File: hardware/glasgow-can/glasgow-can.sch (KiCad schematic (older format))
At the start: 19 parts, among them J1 2834077-2, J10 pkl_jumper_nc, J11 pkl_jumper_nc, J12 pkl_jumper_nc, J13 pkl_jumper_nc, J14 pkl_jumper_nc, J15 pkl_jumper_nc, J2 Conn_01x03_Male, J3 Conn_01x09_Male, J4 A-DS 09 A/KG-T2S, J5 Conn_02x10_Odd_Even, J6 2834077-2, J7 Conn_01x03_Male, J8 Conn_01x09_Male, J9 A-DS 09 A/KG-T2S

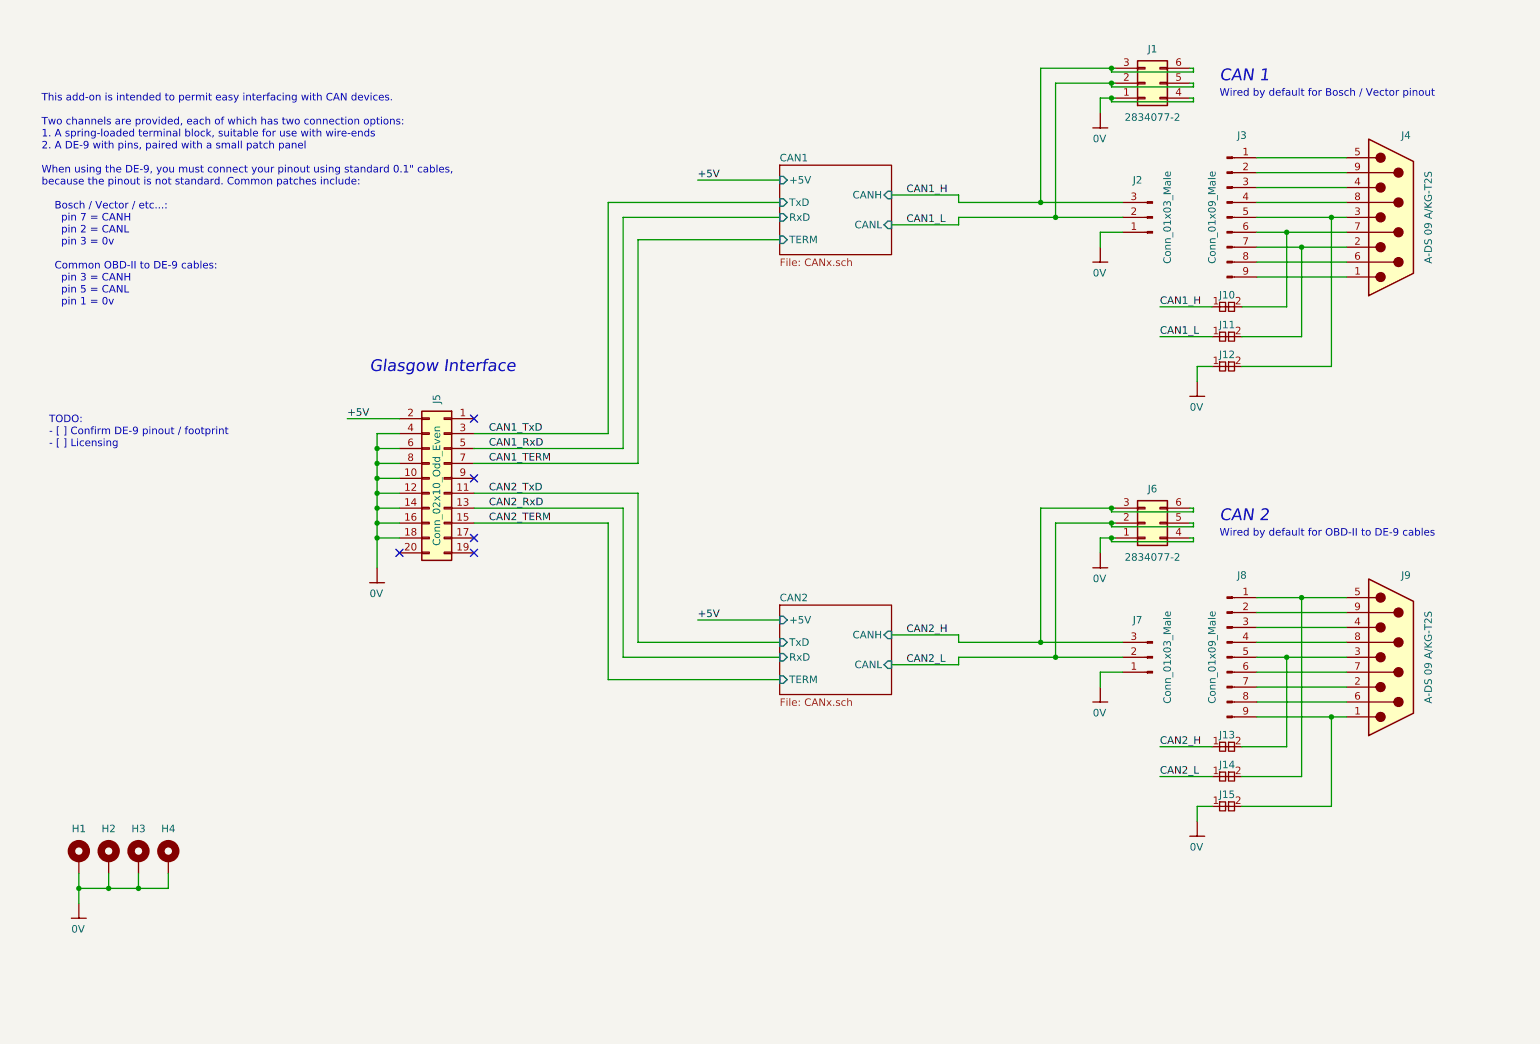
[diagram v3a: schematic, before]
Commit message: fix DE-9 footprint, spruce up schematic and layout
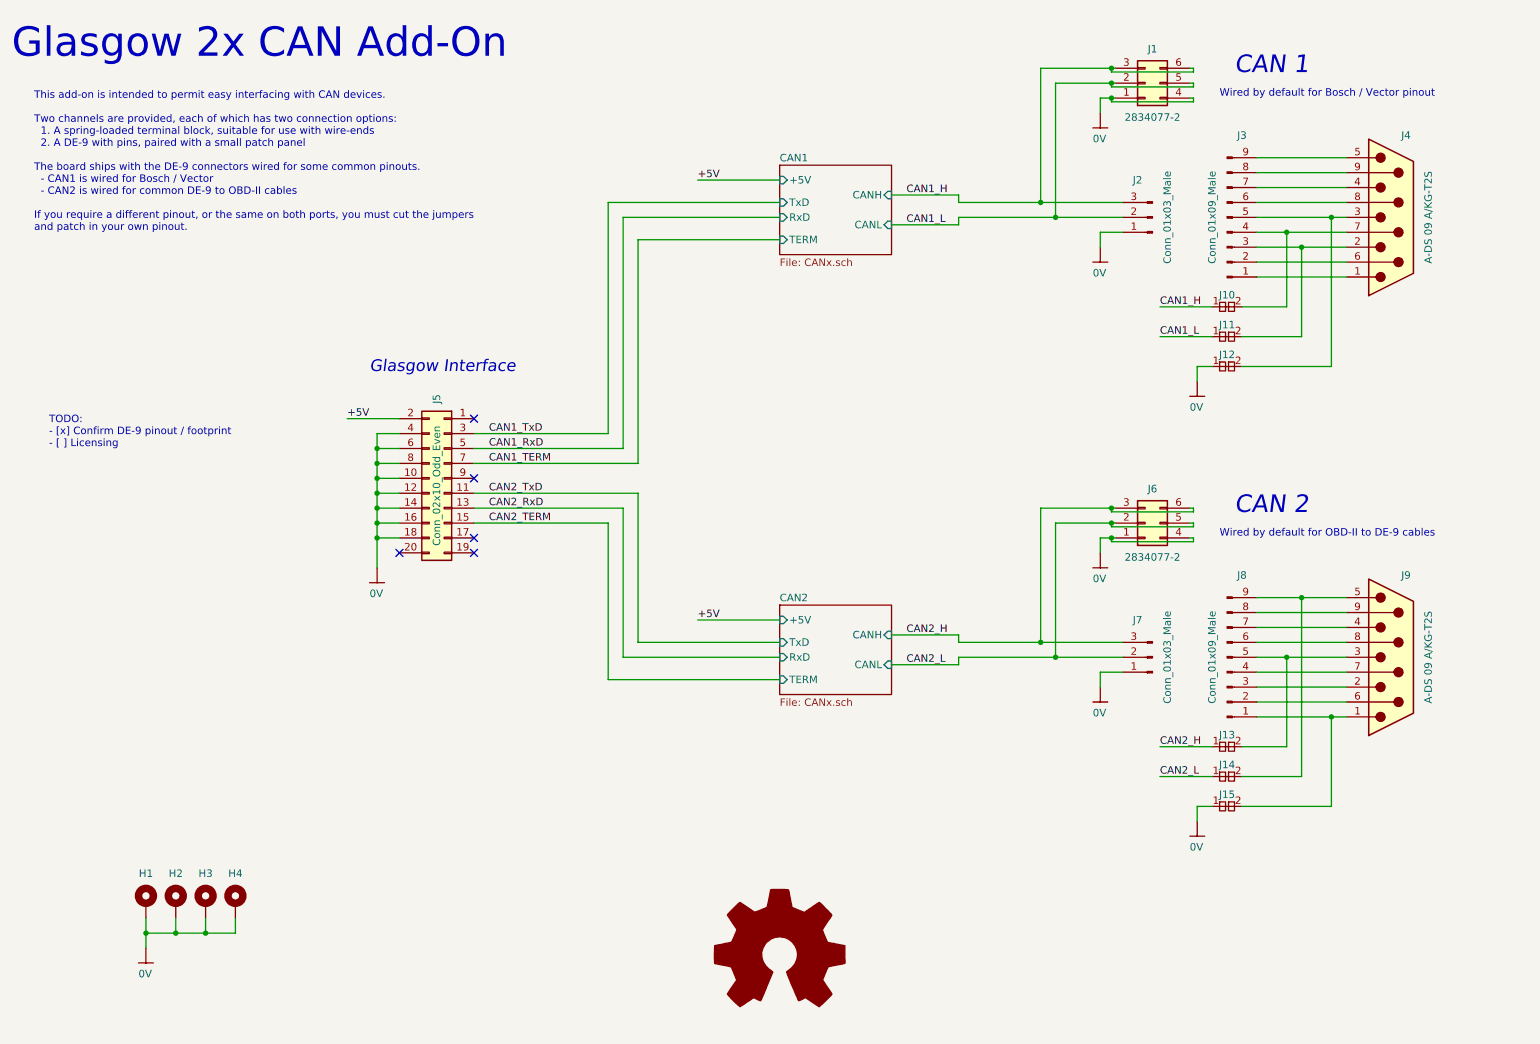
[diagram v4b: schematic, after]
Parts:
- J4, J9: footprint Connector_Dsub:DSUB-9_Female_Horizontal_P2.77x2.84mm_EdgePinOffset7.70mm_Housed_MountingHolesOffset9.12mm -> Connector_Dsub:DSUB-9_Male_Horizontal_P2.77x2.84mm_EdgePinOffset7.70mm_Housed_MountingHolesOffset9.12mm
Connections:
- net at J4.1: now also J3.1 (Pin_1); no longer J3.9 (Pin_9)
- net at J11.2, J4.2: now also J3.3 (Pin_3); no longer J3.7 (Pin_7)
- net at J4.4: now also J3.7 (Pin_7); no longer J3.3 (Pin_3)
- net at J4.5: now also J3.9 (Pin_9); no longer J3.1 (Pin_1)
- net at J4.6: now also J3.2 (Pin_2); no longer J3.8 (Pin_8)
- net at J10.2, J4.7: now also J3.4 (Pin_4); no longer J3.6 (Pin_6)
- net at J4.8: now also J3.6 (Pin_6); no longer J3.4 (Pin_4)
- net at J4.9: now also J3.8 (Pin_8); no longer J3.2 (Pin_2)
- net at J15.2, J9.1: now also J8.1 (Pin_1); no longer J8.9 (Pin_9)
- net at J9.2: now also J8.3 (Pin_3); no longer J8.7 (Pin_7)
- net at J9.4: now also J8.7 (Pin_7); no longer J8.3 (Pin_3)
- net at J14.2, J9.5: now also J8.9 (Pin_9); no longer J8.1 (Pin_1)
- net at J9.6: now also J8.2 (Pin_2); no longer J8.8 (Pin_8)
- net at J9.7: now also J8.4 (Pin_4); no longer J8.6 (Pin_6)
- net at J9.8: now also J8.6 (Pin_6); no longer J8.4 (Pin_4)
- net at J9.9: now also J8.8 (Pin_8); no longer J8.2 (Pin_2)
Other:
- note added: "Glasgow 2x CAN Add-On"
- note added: "TODO:\n- [x] Confirm DE-9 pinout / footprint\n- [ ] Licensing"
- note added: "This add-on is intended to permit easy interfacing with CAN devices.\n\nTwo channels are provided, each of which has two connection options:\n 1. A spring-loaded terminal block, suitable for use with wire-ends\n 2. A DE-9 with pins, paired with a small patch panel\n\nThe board ships with the DE-9 connectors wired for some common pinouts.\n - CAN1 is wired for Bosch / Vector\n - CAN2 is wired for 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"
- note removed: "TODO:\n- [ ] Confirm DE-9 pinout / footprint\n- [ ] Licensing"
- note removed: "This add-on is intended to permit easy interfacing with CAN devices.\n\nTwo channels are provided, each of which has two connection options:\n1. A spring-loaded terminal block, suitable for use with wire-ends\n2. A DE-9 with pins, paired with a small patch panel\n\nWhen using the DE-9, you must connect your pinout using standard 0.1" cables,\nbecause the pinout is not standard. Common patches inc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"
- moved on the sheet: H1, H2, H3, H4
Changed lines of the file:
@@
 F 0 "J4" H 10300 2750 50  0000 C CNN
 F 1 "A-DS 09 A/KG-T2S" V 10450 2200 50  0000 C CNN
-F 2 "Connector_Dsub:DSUB-9_Female_Horizontal_P2.77x2.84mm_EdgePinOffset7.70mm_Housed_MountingHolesOffset9.12mm" H 10200 2200 50  0001 C CNN
+F 2 "Connector_Dsub:DSUB-9_Male_Horizontal_P2.77x2.84mm_EdgePinOffset7.70mm_Housed_MountingHolesOffset9.12mm" H 10200 2200 50  0001 C CNN
 F 3 " ~" H 10200 2200 50  0001 C CNN
 F 4 "Assmann WSW Components" H 10200 2200 50  0001 C CNN "MFR"
@@
 U 1 1 5FCF8B9B
 P 9100 2200
-F 0 "J3" H 9200 2750 50  0000 C CNN
+F 0 "J3" H 9200 1650 50  0000 C CNN
 F 1 "Conn_01x09_Male" V 9000 2200 50  0000 C CNN
 F 2 "Connector_PinHeader_2.54mm:PinHeader_1x09_P2.54mm_Vertical" H 9100 2200 50  0001 C CNN
 F 3 "~" H 9100 2200 50  0001 C CNN
 	1    9100 2200
-	1    0    0    -1
+	1    0    0    1
 $EndComp
 Wire Wire Line
@@
 F 0 "J9" H 10300 5700 50  0000 C CNN
 F 1 "A-DS 09 A/KG-T2S" V 10450 5150 50  0000 C CNN
-F 2 "Connector_Dsub:DSUB-9_Female_Horizontal_P2.77x2.84mm_EdgePinOffset7.70mm_Housed_MountingHolesOffset9.12mm" H 10200 5150 50  0001 C CNN
+F 2 "Connector_Dsub:DSUB-9_Male_Horizontal_P2.77x2.84mm_EdgePinOffset7.70mm_Housed_MountingHolesOffset9.12mm" H 10200 5150 50  0001 C CNN
 F 3 " ~" H 10200 5150 50  0001 C CNN
 F 4 "Assmann WSW Components" H 10200 5150 50  0001 C CNN "MFR"
@@
 U 1 1 5FD1E488
 P 9100 5150
-F 0 "J8" H 9200 5700 50  0000 C CNN
+F 0 "J8" H 9200 4600 50  0000 C CNN
 F 1 "Conn_01x09_Male" V 9000 5150 50  0000 C CNN
 F 2 "Connector_PinHeader_2.54mm:PinHeader_1x09_P2.54mm_Vertical" H 9100 5150 50  0001 C CNN
 F 3 "~" H 9100 5150 50  0001 C CNN
 	1    9100 5150
-	1    0    0    -1
+	1    0    0    1
 $EndComp
 Wire Wire Line
@@
 Wire Wire Line
 	5150 2350 6100 2350
-Text Notes 1150 2800 0    50   ~ 0
-This add-on is intended to permit easy interfacing with CAN devices.\n\nTwo channels are provided, each of which has two connection options:\n1. A spring-loaded terminal block, suitable for use with wire-ends\n2. A DE-9 with pins, paired with a small patch panel\n\nWhen using the DE-9, you must connect your pinout using standard 0.1" cables,\nbecause the pinout is not standard. Common patches include:\n\n    Bosch / Vector / etc...:\n      pin 7 = CANH\n      pin 2 = CANL\n      pin 3 = 0v\n\n    Common OBD-II to DE-9 cables:\n      pin 3 = CANH\n      pin 5 = CANL\n      pin 1 = 0v
-Text Notes 9050 1300 0    79   Italic 0
+Text Notes 1100 2300 0    50   ~ 0
+This add-on is intended to permit easy interfacing with CAN devices.\n\nTwo channels are provided, each of which has two connection options:\n  1. A spring-loaded terminal block, suitable for use with wire-ends\n  2. A DE-9 with pins, paired with a small patch panel\n\nThe board ships with the DE-9 connectors wired for some common pinouts.\n  - CAN1 is wired for Bosch / Vector\n  - CAN2 is wired for common DE-9 to OBD-II cables\n\nIf you require a different pinout, or the same on both ports, you must cut the jumpers\nand patch in your own pinout.
+Text Notes 9150 1250 0    118  Italic 0
 CAN 1
-Text Notes 9050 4250 0    79   Italic 0
+Text Notes 9150 4200 0    118  Italic 0
 CAN 2
 Wire Wire Line
@@
 L Mechanical:MountingHole_Pad H1
 U 1 1 5FF2F90D
-P 1400 6500
-F 0 "H1" H 1400 6700 50  0000 C CNN
-F 1 "MountingHole_Pad" H 1500 6458 50  0001 L CNN
-F 2 "MountingHole:MountingHole_3.2mm_M3_Pad_Via" H 1400 6500 50  0001 C CNN
-F 3 "~" H 1400 6500 50  0001 C CNN
-	1    1400 6500
+P 1850 6800
+F 0 "H1" H 1850 7000 50  0000 C CNN
+F 1 "MountingHole_Pad" H 1950 6758 50  0001 L CNN
+F 2 "MountingHole:MountingHole_3.2mm_M3_Pad_Via" H 1850 6800 50  0001 C CNN
+F 3 "~" H 1850 6800 50  0001 C CNN
+	1    1850 6800
 	1    0    0    -1
 $EndComp
@@
 L Mechanical:MountingHole_Pad H2
 U 1 1 5FF30176
-P 1600 6500
-F 0 "H2" H 1600 6700 50  0000 C CNN
-F 1 "MountingHole_Pad" H 1700 6458 50  0001 L CNN
-F 2 "MountingHole:MountingHole_3.2mm_M3_Pad_Via" H 1600 6500 50  0001 C CNN
-F 3 "~" H 1600 6500 50  0001 C CNN
-	1    1600 6500
+P 2050 6800
+F 0 "H2" H 2050 7000 50  0000 C CNN
+F 1 "MountingHole_Pad" H 2150 6758 50  0001 L CNN
+F 2 "MountingHole:MountingHole_3.2mm_M3_Pad_Via" H 2050 6800 50  0001 C CNN
+F 3 "~" H 2050 6800 50  0001 C CNN
+	1    2050 6800
 	1    0    0    -1
 $EndComp
@@
 L Mechanical:MountingHole_Pad H3
 U 1 1 5FF30358
-P 1800 6500
-F 0 "H3" H 1800 6700 50  0000 C CNN
-F 1 "MountingHole_Pad" H 1900 6458 50  0001 L CNN
-F 2 "MountingHole:MountingHole_3.2mm_M3_Pad_Via" H 1800 6500 50  0001 C CNN
-F 3 "~" H 1800 6500 50  0001 C CNN
-	1    1800 6500
+P 2250 6800
+F 0 "H3" H 2250 7000 50  0000 C CNN
+F 1 "MountingHole_Pad" H 2350 6758 50  0001 L CNN
+F 2 "MountingHole:MountingHole_3.2mm_M3_Pad_Via" H 2250 6800 50  0001 C CNN
+F 3 "~" H 2250 6800 50  0001 C CNN
+	1    2250 6800
 	1    0    0    -1
 $EndComp
@@
 L Mechanical:MountingHole_Pad H4
 U 1 1 5FF30540
-P 2000 6500
-F 0 "H4" H 2000 6700 50  0000 C CNN
-F 1 "MountingHole_Pad" H 2100 6458 50  0001 L CNN
-F 2 "MountingHole:MountingHole_3.2mm_M3_Pad_Via" H 2000 6500 50  0001 C CNN
-F 3 "~" H 2000 6500 50  0001 C CNN
-	1    2000 6500
+P 2450 6800
+F 0 "H4" H 2450 7000 50  0000 C CNN
+F 1 "MountingHole_Pad" H 2550 6758 50  0001 L CNN
+F 2 "MountingHole:MountingHole_3.2mm_M3_Pad_Via" H 2450 6800 50  0001 C CNN
+F 3 "~" H 2450 6800 50  0001 C CNN
+	1    2450 6800
 	1    0    0    -1
 $EndComp
@@
 L DX_MON:0V #PWR018
 U 1 1 5FF307BA
-P 1400 6800
-F 0 "#PWR018" H 1400 6600 50  0001 C CNN
-F 1 "0V" H 1405 6627 50  0000 C CNN
-F 2 "" H 1100 6900 50  0001 C CNN
-F 3 "" H 1100 6900 50  0001 C CNN
-	1    1400 6800
+P 1850 7100
+F 0 "#PWR018" H 1850 6900 50  0001 C CNN
+F 1 "0V" H 1855 6927 50  0000 C CNN
+F 2 "" H 1550 7200 50  0001 C CNN
+F 3 "" H 1550 7200 50  0001 C CNN
+	1    1850 7100
 	-1   0    0    -1
 $EndComp
 Wire Wire Line
-	1400 6600 1400 6700
-Wire Wire Line
-	1400 6700 1600 6700
-Wire Wire Line
-	1600 6700 1600 6600
-Connection ~ 1400 6700
-Wire Wire Line
-	1400 6700 1400 6800
-Wire Wire Line
-	1800 6700 1800 6600
-Wire Wire Line
-	1800 6700 2000 6700
-Wire Wire Line
-	2000 6700 2000 6600
-Connection ~ 1800 6700
-Wire Wire Line
-	1600 6700 1800 6700
-Connection ~ 1600 6700
+	1850 6900 1850 7000
+Wire Wire Line
+	1850 7000 2050 7000
+Wire Wire Line
+	2050 7000 2050 6900
+Connection ~ 1850 7000
+Wire Wire Line
+	1850 7000 1850 7100
+Wire Wire Line
+	2250 7000 2250 6900
+Wire Wire Line
+	2250 7000 2450 7000
+Wire Wire Line
+	2450 7000 2450 6900
+Connection ~ 2250 7000
+Wire Wire Line
+	2050 7000 2250 7000
+Connection ~ 2050 7000
 Text Notes 1200 3750 0    50   ~ 0
-TODO:\n- [ ] Confirm DE-9 pinout / footprint\n- [ ] Licensing
+TODO:\n- [x] Confirm DE-9 pinout / footprint\n- [ ] Licensing
+Text Notes 950  1150 0    197  ~ 0
+Glasgow 2x CAN Add-On
+$Comp
+L Graphic:Logo_Open_Hardware_Large #LOGO?
+U 1 1 5FD20AE9
+P 6100 7150
+F 0 "#LOGO?" H 6100 7650 50  0001 C CNN
+F 1 "Logo_Open_Hardware_Large" H 6100 6750 50  0001 C CNN
+F 2 "" H 6100 7150 50  0001 C CNN
+F 3 "~" H 6100 7150 50  0001 C CNN
+	1    6100 7150
+	1    0    0    -1
+$EndComp
 $EndSCHEMATC

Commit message: fixup README, and other misc changes
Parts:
- added LOGO1: Logo_Open_Hardware_Large, Symbol:OSHW-Logo2_7.3x6mm_SilkScreen, symbol Graphic:Logo_Open_Hardware_Large
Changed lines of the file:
@@
 Glasgow 2x CAN Add-On
 $Comp
-L Graphic:Logo_Open_Hardware_Large #LOGO?
+L Graphic:Logo_Open_Hardware_Large LOGO1
 U 1 1 5FD20AE9
 P 6100 7150
-F 0 "#LOGO?" H 6100 7650 50  0001 C CNN
+F 0 "LOGO1" H 6100 7650 50  0001 C CNN
 F 1 "Logo_Open_Hardware_Large" H 6100 6750 50  0001 C CNN
-F 2 "" H 6100 7150 50  0001 C CNN
+F 2 "Symbol:OSHW-Logo2_7.3x6mm_SilkScreen" H 6100 7150 50  0001 C CNN
 F 3 "~" H 6100 7150 50  0001 C CNN
 	1    6100 7150

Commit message: minor tweaks
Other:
- note added: "BSD-3-Clause"
- note removed: "TODO:\n- [x] Confirm DE-9 pinout / footprint\n- [ ] Licensing"
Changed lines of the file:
@@
 Sheet 1 3
 Title "Glasgow CAN Add-On"
-Date "2020-11-20"
+Date "2020-12-19"
 Rev "r0"
 Comp ""
@@
 	2050 7000 2250 7000
 Connection ~ 2050 7000
-Text Notes 1200 3750 0    50   ~ 0
-TODO:\n- [x] Confirm DE-9 pinout / footprint\n- [ ] Licensing
 Text Notes 950  1150 0    197  ~ 0
 Glasgow 2x CAN Add-On
@@
 	1    0    0    -1
 $EndComp
+Text Notes 5800 7650 0    50   ~ 0
+BSD-3-Clause
 $EndSCHEMATC
